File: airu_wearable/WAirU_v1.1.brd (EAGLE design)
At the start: 43.8 x 51.7 mm, 50 parts, among them Q2 MMBT3904LT1G, Q3 MMBT3904LT1G, Q6 BSS84, U2 CN3065-DFN8, U3 HDC1080DMBT, U4 PAM2305AABADJ, U6 PAM2401, U7 ESP32_WROOM32_SKINNY

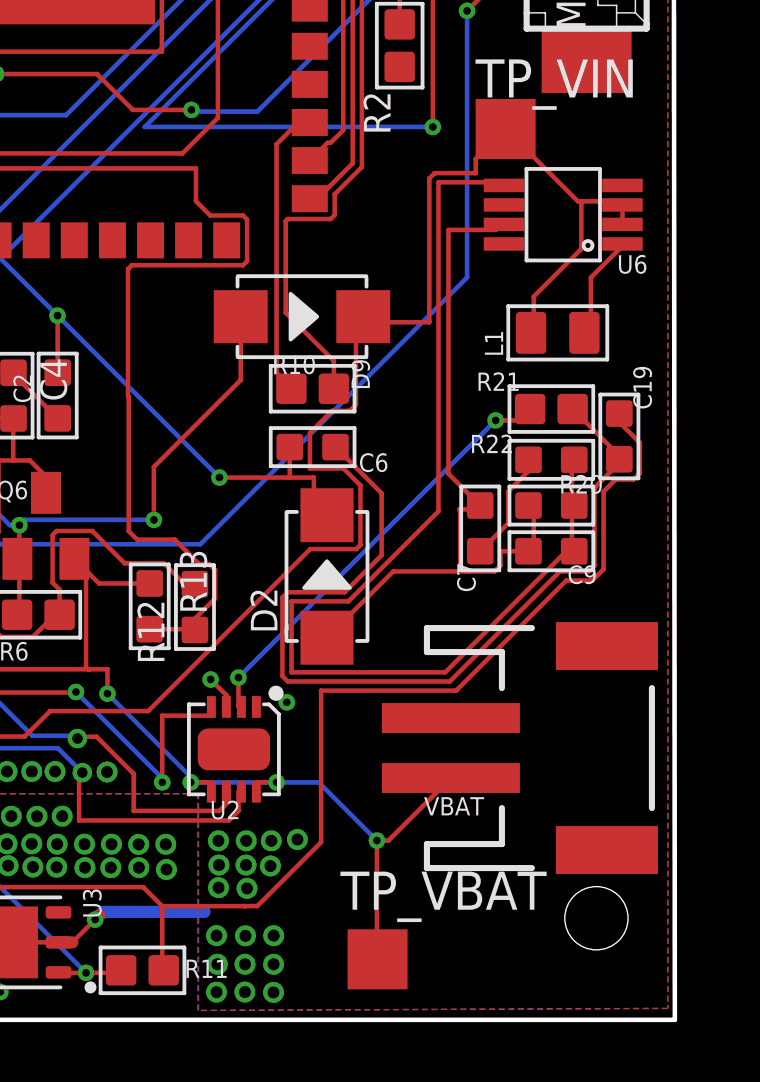
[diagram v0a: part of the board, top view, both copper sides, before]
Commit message: Adjusted the battery connector away from mounting hole
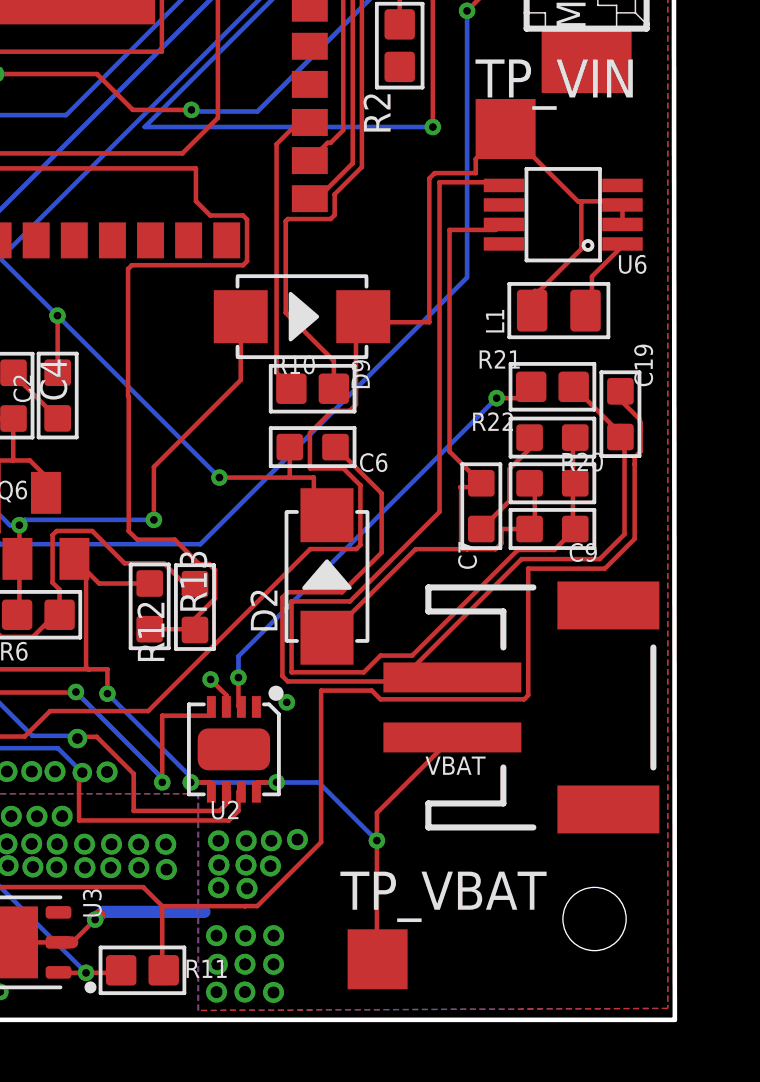
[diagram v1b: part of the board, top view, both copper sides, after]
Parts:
- moved VBAT 1.35 mm to (48.0, 8.85)
- moved C19 0.74 mm to (49.9, 18.6)
- moved C9 0.74 mm to (47.6, 14.8)
- moved R22 0.74 mm to (47.6, 17.8)
- moved C7 0.74 mm to (45.2, 15.6)
- moved L1 0.74 mm to (47.8, 22.1)
- moved R21 0.74 mm to (47.6, 19.5)
- moved R20 0.74 mm to (47.6, 16.3)
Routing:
- net 3.3V: track 124.1 -> 127.2 mm
- net GND: track 68.3 -> 71.3 mm
- net VBAT: track 34.0 -> 35.2 mm
- net N$6: track 14.7 -> 15.4 mm
- net N$3: track 3.45 -> 2.69 mm
- net V_IN: track 124.0 -> 123.3 mm
- net N$10: track 35.9 -> 36.5 mm

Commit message: Remove pull down on PM_SET line
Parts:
- removed R9: 4.7K, Seeed-Resistor:R0603
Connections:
- net GND: no longer R9.1
- net PM_SET: no longer R9.2
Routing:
- net PM_SET: track 19.8 -> 18.0 mm

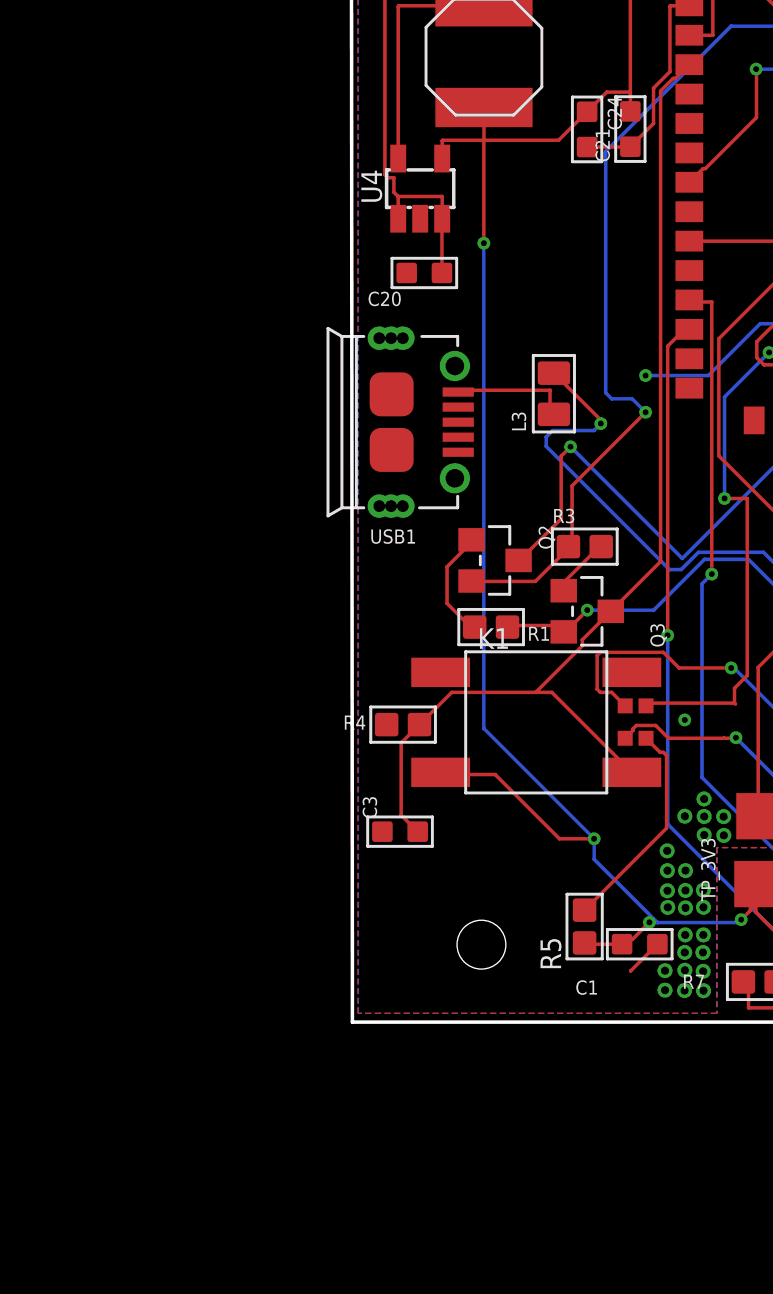
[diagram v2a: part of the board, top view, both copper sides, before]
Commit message: Fix Schematic for #9, #10, #11, #12 on github opening issue
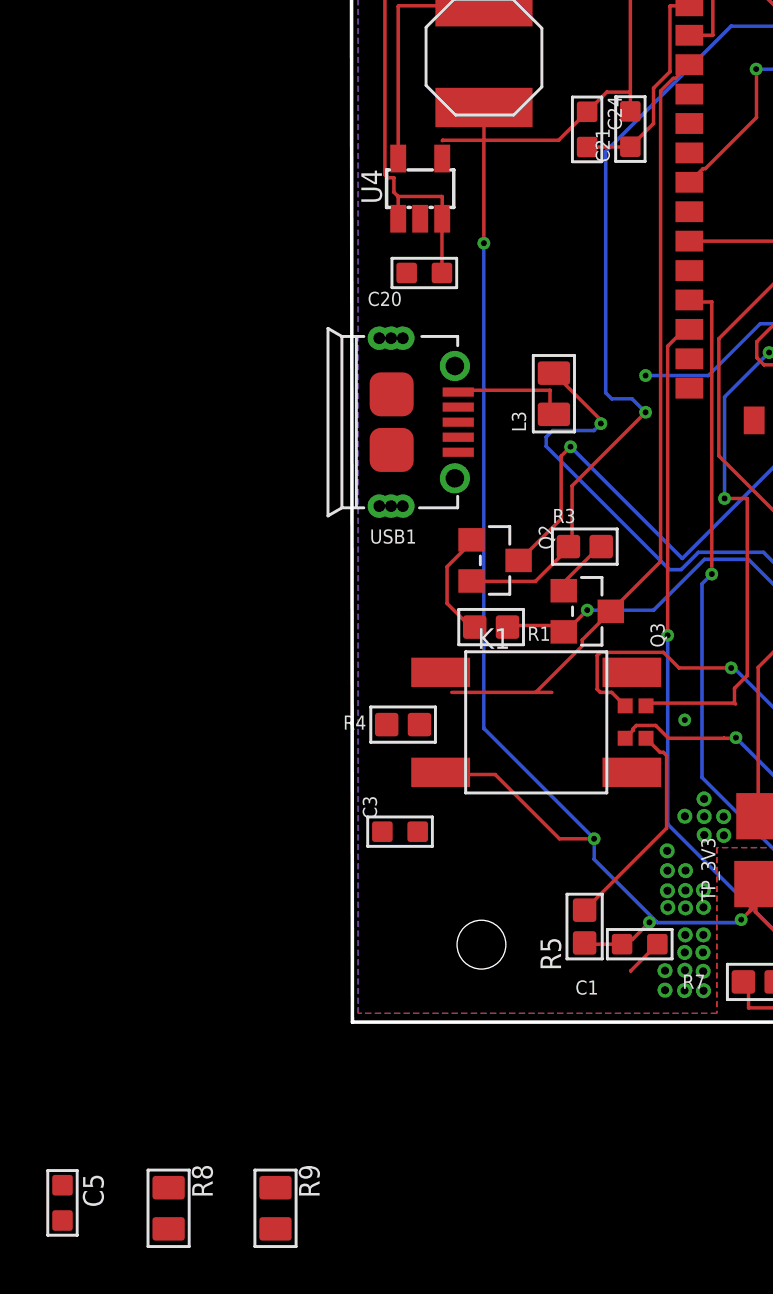
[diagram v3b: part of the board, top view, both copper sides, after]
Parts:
- added C5: 100pf, OPL_Capacitor:C0603
- added R8: 2.2K, OPL_Resistor:R0805
- added R9: 10K, OPL_Resistor:R0805
- C10, C7, C9: value 22uf -> 10uf
- R12, R13, R22: value 100K -> 100K 1/10W
- R20: value 750K -> 100K 1/10W
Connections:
- new net N$22: C5.1, R8.2, R9.1, U4.4
- net 3.3V: now also C5.2, R4.1, R9.2; no longer K1.2, U4.4
- net GND: now also K1.3, R8.1; no longer R4.1
- net RESET: now also K1.1; no longer K1.3
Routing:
- net RESET: track 46.3 -> 34.2 mm
- net 3.3V: track 127.2 -> 126.3 mm

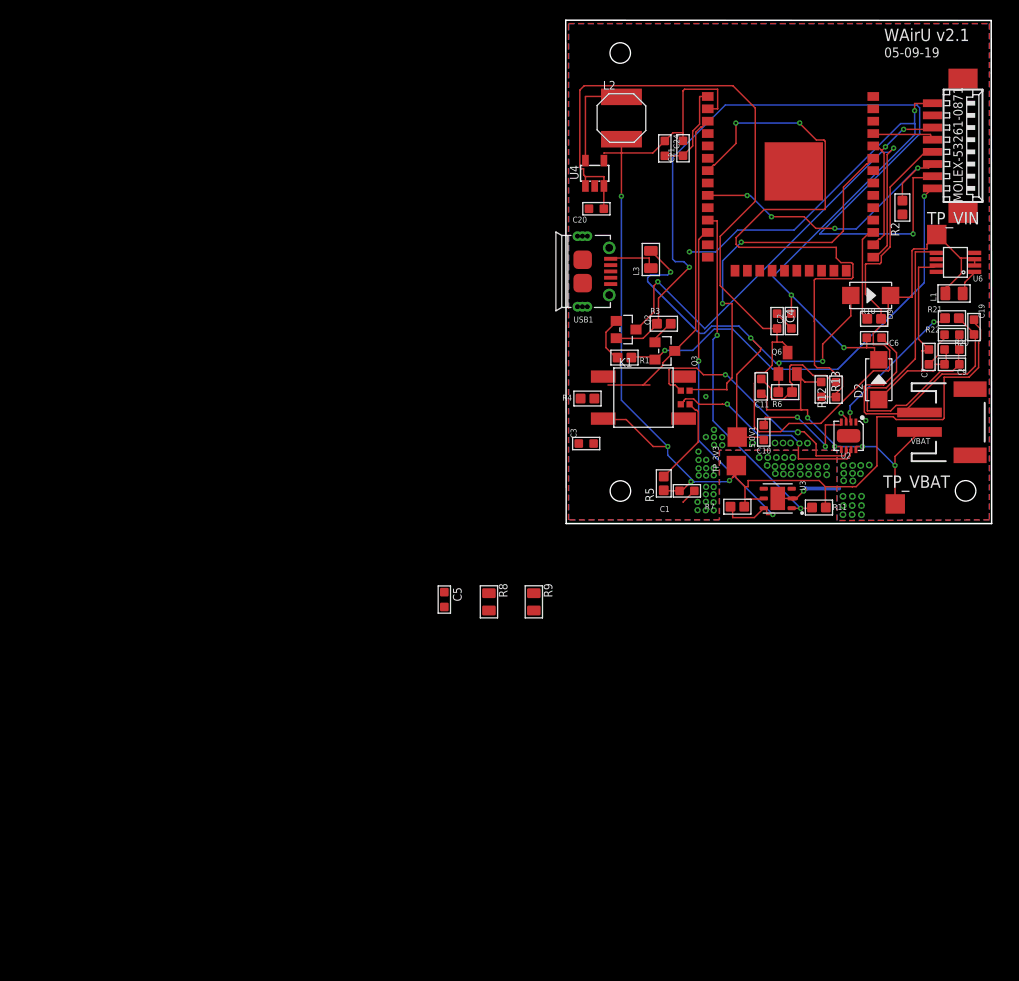
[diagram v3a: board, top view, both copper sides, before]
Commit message: Added Switch circuit PAM2401 input for VBUS and VBAT. Added voltage divider for PAM2401 output
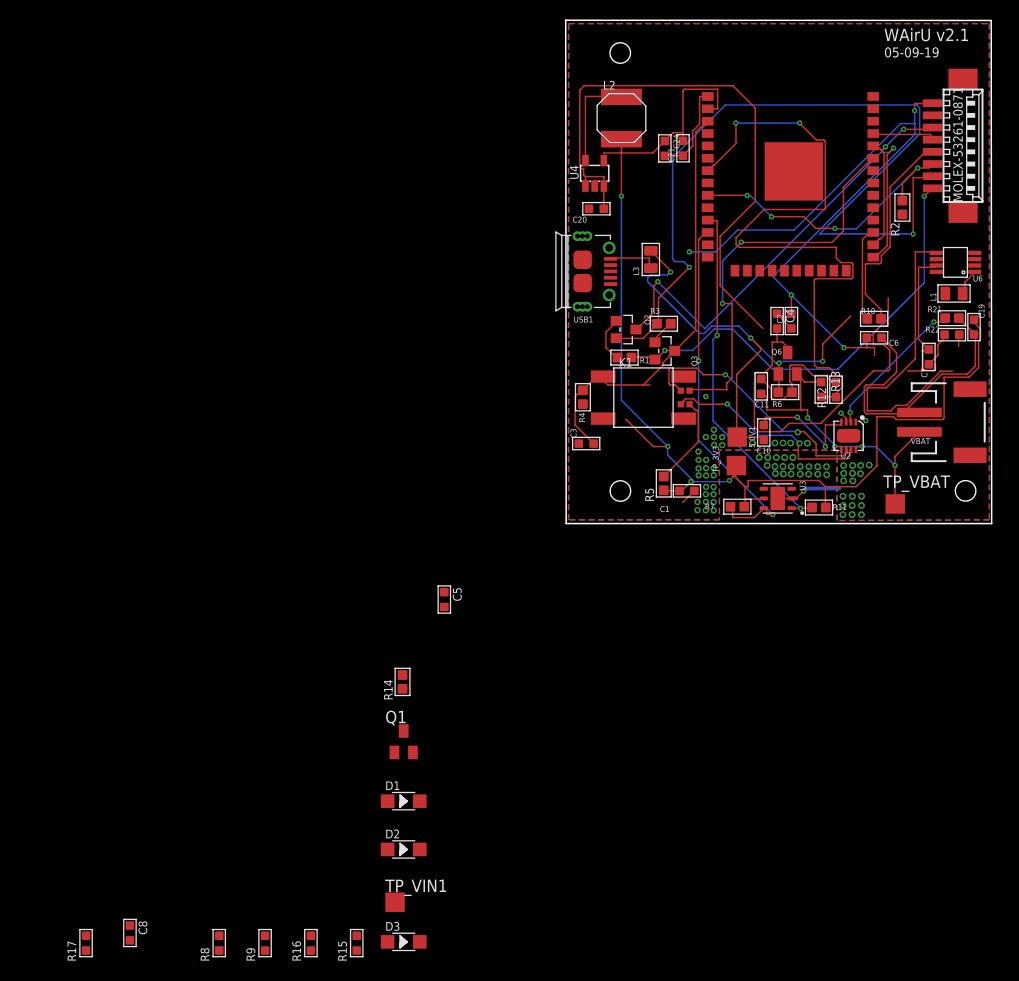
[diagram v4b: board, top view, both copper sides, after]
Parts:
- removed C9: 10uf, OPL_Capacitor:C0603
- removed D9: 40V-1A, Seeed-Diode:DO-214AC
- removed R20: 100K 1/10W, OPL_Resistor:R0603
- removed TP_VIN: TPTP20SQ, testpad:TP20SQ
- added C8: 22uf, OPL_Capacitor:C0603
- added D1, D3: 20V-1A, Seeed-OPL-Diode:SOD-123
- added Q1: BSS123, transistor-small-signal:SOT23
- added R14: 100K 1/10W, Seeed-Resistor:R0603
- added R15: 680K, Seeed-OPL-Resistor:R0603
- added R16: 69.8K 1/10W, Seeed-OPL-Resistor:R0603
- added R17: 120K, Seeed-OPL-Resistor:R0603
- added TP_VIN1: TPTP20SQ, testpad:TP20SQ
- C7: value 10uf -> 22uf
- D2: value 40V-1A -> 20V-1A; device Seeed-Diode:DO-214AC -> Seeed-OPL-Diode:SOD-123
- R8: value 2.2K -> 69.8K 1/10W; device OPL_Resistor:R0805 -> Seeed-OPL-Resistor:R0603
- R9: value 10K -> 470K; device OPL_Resistor:R0805 -> Seeed-OPL-Resistor:R0603
- moved D2 68.6 mm to (-8.71, -35.0), turned to 0 degrees
- moved R8 44.7 mm to (-27.7, -44.7)
- moved R9 44.6 mm to (-23.0, -44.7)
- moved R4 0.49 mm to (9.70, 11.4), turned to 180 degrees
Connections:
- net PM_SET renamed PM_SET/TXD0
- net RXD renamed RXD0
- net TXD renamed PMS_TX
- new net N$24: R15.2, R16.2
- new net N$67: C4.2, L1.1, Q1.3, R14.1, TP_VIN1.TP, U6.2, U6.3
- new net N$82: R8.1, R9.1
- net 5.0V: now also D1.-, D2.-; no longer D2.2
- net GND: now also Q1.2, R17.1; no longer R8.1
- net N$10: now also C8.1, R16.1; no longer C9.1, R20.1
- net N$22: now also R17.2; no longer R9.1
- net N$4: now also C8.2, D2.+, R15.1; no longer C9.2, D2.1, R20.2
- net VBAT: now also R14.2
- net VBUS: now also D1.+, D3.+, Q1.1; no longer D9.1
- net V_IN: now also D3.-; no longer C4.2, D9.2, L1.1, TP_VIN.TP, U6.2, U6.3
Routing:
- net V_IN: track 123.3 -> 100.7 mm
- net RESET: track 34.2 -> 44.7 mm
- net N$4: track 24.3 -> 17.1 mm
- net N$10: track 36.5 -> 33.4 mm
- net 3.3V: track 126.3 -> 124.1 mm
- net VBUS: track 54.5 -> 52.3 mm
- net 5.0V: track 72.2 -> 71.6 mm

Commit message: 100kOhm PD on Q1 Removed D1 C10 decoupling grounded PMRST to GPIO2 U2RXD to GPIO13
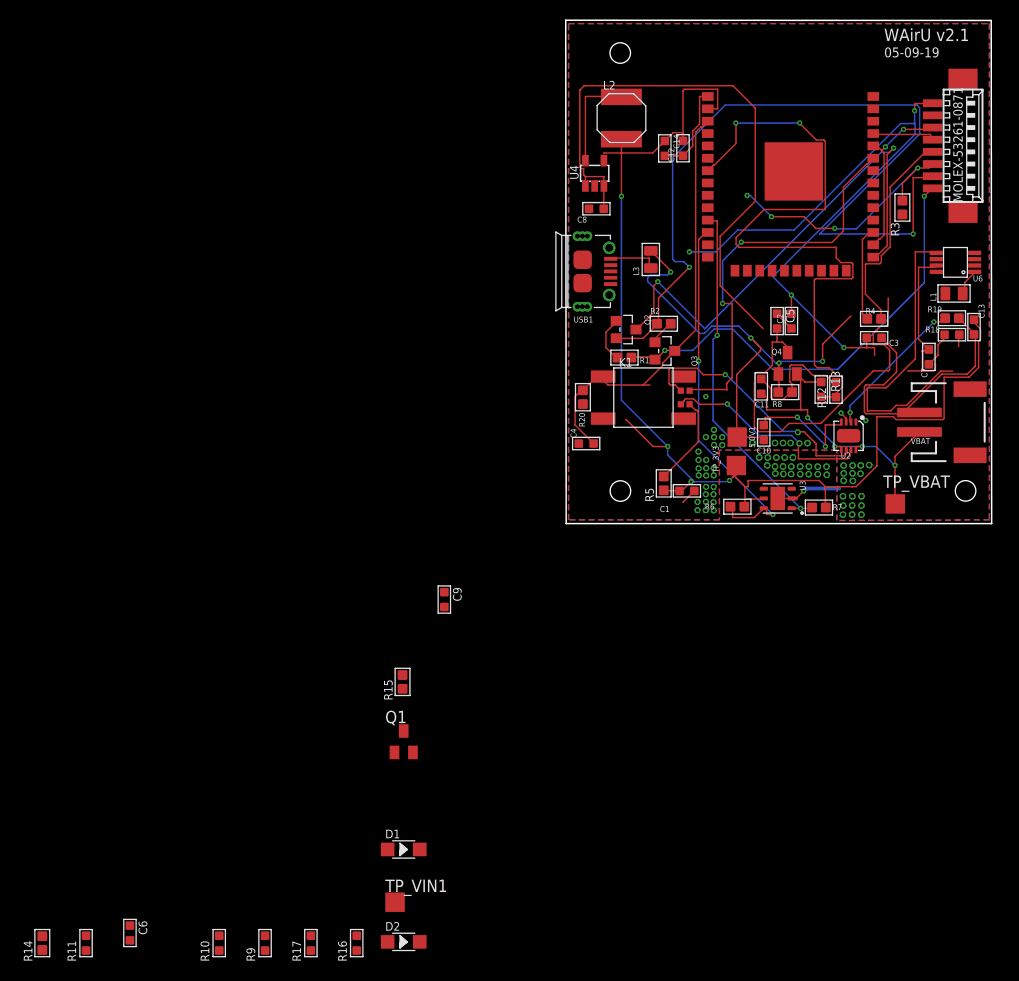
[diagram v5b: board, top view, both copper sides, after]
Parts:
- removed C20: 10uf, Seeed-Capacitor:C0603
- removed D3: 20V-1A, Seeed-OPL-Diode:SOD-123
- added C9: 100pf, OPL_Capacitor:C0603
- added R20: 10K, Seeed-Resistor:R0603
- C4: value 10uf -> 1uf
- C5: value 100pf -> 10uf; device OPL_Capacitor:C0603 -> Seeed-Capacitor:C0603
- C6: value 1uf -> 22uf; device Seeed-Capacitor:C0603 -> OPL_Capacitor:C0603
- C8: value 22uf -> 10uf; device OPL_Capacitor:C0603 -> Seeed-Capacitor:C0603
- R10: value 220R -> 69.8K 1/10W; device Seeed-Resistor:R0603 -> Seeed-OPL-Resistor:R0603
- R11: value 4.7K -> 120K; device Seeed-Resistor:R0603 -> Seeed-OPL-Resistor:R0603
- R15: value 680K -> 100K 1/10W; device Seeed-OPL-Resistor:R0603 -> Seeed-Resistor:R0603
- R16: value 69.8K 1/10W -> 680K
- R17: value 120K -> 69.8K 1/10W
- R2: value 4.7K -> 10K
- R3: value 10K -> 4.7K
- R4: value 10K -> 220R
- R6: value 100K 1/10W -> 4.7K
- R8: value 69.8K 1/10W -> 100K 1/10W; device Seeed-OPL-Resistor:R0603 -> Seeed-Resistor:R0603
- moved C6 97.9 mm to (-36.8, -43.6), turned to 0 degrees
- moved R10 93.0 mm to (-27.7, -44.7), turned to 0 degrees
- moved C8 88.5 mm to (11.1, 30.8), turned to 90 degrees
- moved R11 87.6 mm to (-41.4, -44.7), turned to 0 degrees
- moved R8 81.2 mm to (30.5, 11.9), turned to 270 degrees
- moved R14 45.7 mm to (-45.8, -44.7)
- moved C5 44.6 mm to (29.6, 19.2)
- moved C3 31.5 mm to (39.6, 17.5), turned to 270 degrees
- moved R4 31.0 mm to (39.6, 19.5), turned to 90 degrees
- moved R2 27.3 mm to (18.0, 19.0), turned to 90 degrees
- moved R3 27.3 mm to (42.5, 30.9), turned to 180 degrees
- moved R15 27.2 mm to (-8.83, -17.8)
- moved C4 23.3 mm to (10.0, 6.66), turned to 90 degrees
- moved R17 23.1 mm to (-18.3, -44.7)
- moved R6 12.8 mm to (25.6, 0.17), turned to 90 degrees
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- renumbered C19 to C13, C21 to C12, C24 to C14, Q6 to Q4, R21 to R19, R22 to R18, U$4 to U1
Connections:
- net PM_SET/TXD0 renamed PM_SET/RXD0
- net RXD0 renamed TXD0
- removed net N$5: C10.1, U2.4
- removed net N$7: U7.16
- net 3.3V: now also C9.2, R20.1, R6.2; no longer C5.2, R11.2, R4.1
- net 5.0V: now also C3.2; no longer C6.2, D1.-, D2.-
- net DTR: now also R2.1; no longer R3.1
- net GND: now also C10.1, C5.1, C8.1, R11.1, R14.1, R3.1, R8.1; no longer C20.1, C6.1, R17.1, R2.1, R6.1
- net N$10: now also C6.1, R17.1; no longer C8.1, R16.1
- net N$12: now also R2.2; no longer R3.2
- net N$22: now also C9.1, R10.2, R11.2; no longer C5.1, R17.2, R8.2
- net N$24: now also R17.2; no longer R15.2
- net N$4: now also C6.2, D1.+, R16.1; no longer C8.2, D2.+, R15.1
- net N$67: now also C5.2, R15.1; no longer C4.2, R14.1
- net N$82: now also R10.1; no longer R8.1
- net PMS_TX: now also R4.2; no longer R10.2
- net PM_RESET: now also R3.2, U7.24; no longer R2.2, U7.9
- net RESET: now also C4.2, R20.2; no longer C3.2, R4.2
- net SCL: now also R6.1; no longer R7.1
- net SDA: now also R7.1; no longer R11.1
- net U2RXD: now also R4.1, U7.16; no longer R10.1, U7.27
- net VBAT: now also R15.2; no longer R14.2
- net VBUS: now also D1.-, D2.+, R14.2, R8.2, U2.4; no longer D1.+, D3.+, R6.2
- net V_IN: now also C8.2, D2.-; no longer C20.2, D3.-
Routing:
- net N$5: track 12.6 -> 0.00 mm, vias 2 -> 0
- net VBUS: track 52.3 -> 64.5 mm, vias 4 -> 6
- net PM_RESET: track 31.3 -> 27.3 mm

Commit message: PCB design
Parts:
- C10: value 10uf -> 22uf; device OPL_Capacitor:C0603 -> Seeed-OPL-Capacitor:C0805
- moved R14 111.9 mm to (47.5, 17.1)
- moved C6 109.3 mm to (49.3, 23.7), turned to 270 degrees
- moved R11 102.7 mm to (13.1, 42.5), turned to 90 degrees
- moved R17 97.2 mm to (49.3, 25.2), turned to 90 degrees
- moved R16 95.1 mm to (49.3, 26.7), turned to 90 degrees
- moved R10 93.5 mm to (13.1, 39.4), turned to 90 degrees
- moved R9 90.1 mm to (13.1, 37.9), turned to 90 degrees
- moved D1 81.9 mm to (42.4, 28.9), turned to 90 degrees
- moved TP_VIN1 76.5 mm to (41.4, 16.5)
- moved D2 76.3 mm to (15.6, 27.7), turned to 90 degrees
- moved Q1 68.4 mm to (44.3, 19.2), turned to 90 degrees
- moved R15 63.6 mm to (44.7, 16.4), turned to 90 degrees
- moved C9 53.3 mm to (13.1, 41.0), turned to 270 degrees
- moved C13 38.8 mm to (18.2, 41.0), turned to 90 degrees
- moved R1 36.0 mm to (42.2, 37.9), turned to 0 degrees
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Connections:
- net N$67 renamed V_IN1
- removed net 5.0V: C2.2, C3.2, MOLEX-53261-0871.8
- net VBUS: now also C2.2, C3.2, MOLEX-53261-0871.8
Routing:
- net GND: track 71.3 -> 203.4 mm
- net VBAT: track 35.2 -> 128.5 mm, vias 4 -> 3
- net VBUS: track 64.5 -> 147.5 mm, vias 6 -> 3
- net V_IN: track 100.7 -> 18.9 mm
- net 5.0V: track 71.6 -> 0.00 mm, vias 4 -> 0
- net DTR: track 87.0 -> 16.7 mm, vias 2 -> 0
- net GPIO0: track 52.0 -> 8.94 mm, vias 2 -> 0
- net RESET: track 44.7 -> 85.3 mm, vias 0 -> 3
- net RTS: track 47.0 -> 10.2 mm, vias 2 -> 0
- net BAT_CHECK: track 69.1 -> 43.7 mm
- net PM_RESET: track 27.3 -> 49.1 mm, vias 4 -> 0
- net U2RXD: track 9.69 -> 31.4 mm, vias 0 -> 2
- net N$10: track 33.4 -> 13.1 mm
- net PM_SET/RXD0: track 18.0 -> 35.0 mm, vias 2 -> 0
- net GP_LED: track 40.9 -> 57.8 mm
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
